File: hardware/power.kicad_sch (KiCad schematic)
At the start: 10 parts, among them J1 Conn_01x02_Pin, U2 TPS7A91

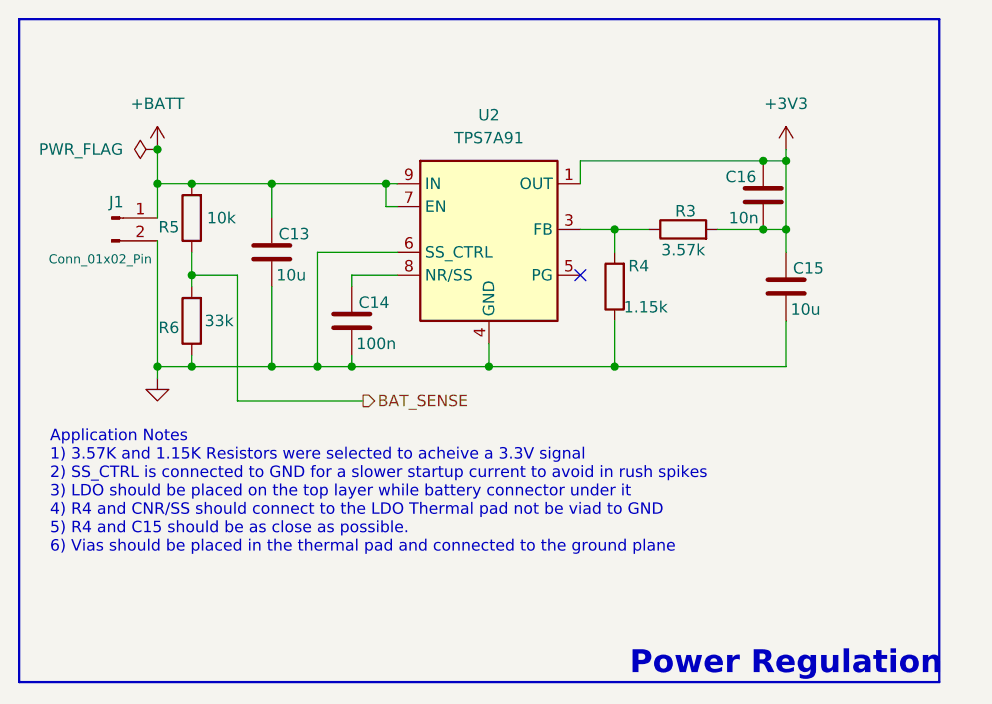
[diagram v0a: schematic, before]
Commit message: feat(kicad): Added step files for missing parts
changed flyback diode to SMA part with 5A max

Redid initial layout
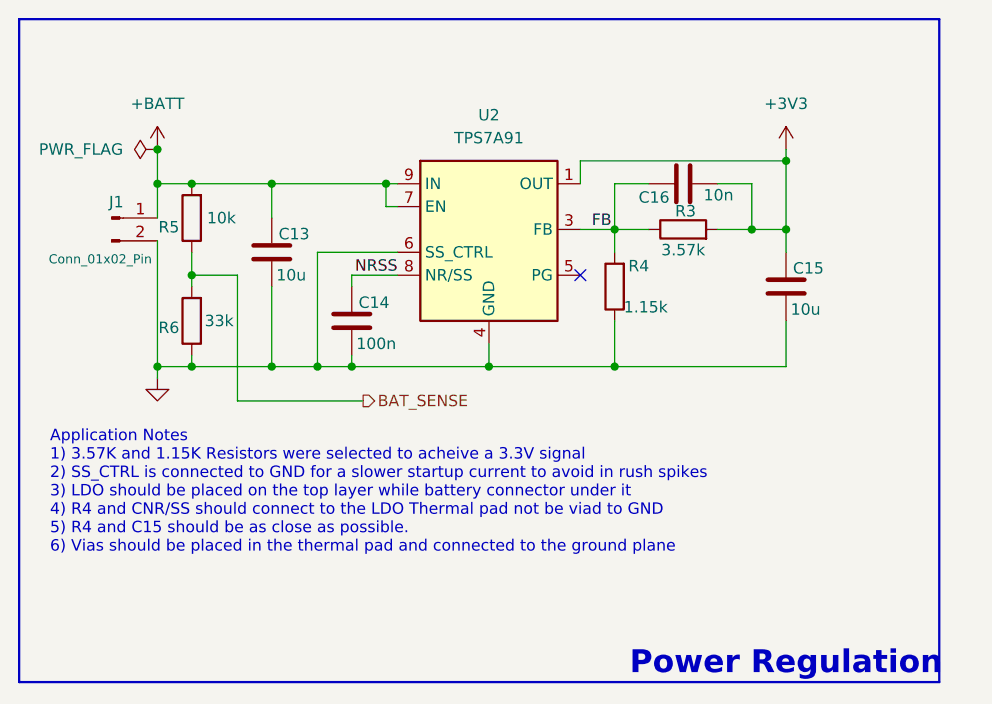
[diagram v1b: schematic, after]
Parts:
- U2: footprint Package_DFN_QFN:Texas_S-PDSO-N10_EP1.2x2mm -> Package_DFN_QFN:Texas_S-PDSO-N10_EP1.2x2mm_ThermalVias
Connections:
- net +3V3: no longer C16.1
- net NRSS: now reaches C14.1, U2.8 (NR/SS)
- net FB: now reaches R3.1, R4.2, U2.3 (FB)
- net FB: now also C16.1
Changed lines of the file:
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@@
+	)
+	(junction
+		(at 170.18 90.17)
+		(diameter 0)
+		(color 0 0 0 0)
 	)
 	(junction
@@
 	)
 	(junction
-		(at 171.45 90.17)
-		(diameter 0)
-		(color 0 0 0 0)
-	)
-	(junction
 		(at 107.95 85.09)
 		(diameter 0)
@@
 	(junction
 		(at 173.99 90.17)
-		(diameter 0)
-		(color 0 0 0 0)
-	)
-	(junction
-		(at 171.45 82.55)
 		(diameter 0)
 		(color 0 0 0 0)
@@
 	(wire
 		(pts
+			(xy 158.75 85.09) (xy 154.94 85.09)
+		)
+		(stroke
+			(width 0)
+			(type default)
+		)
+	)
+	(wire
+		(pts
 			(xy 107.95 104.14) (xy 107.95 105.41)
 		)
@@
 	(wire
 		(pts
-			(xy 171.45 82.55) (xy 173.99 82.55)
+			(xy 151.13 82.55) (xy 173.99 82.55)
 		)
 		(stroke
@@
 	(wire
 		(pts
-			(xy 151.13 82.55) (xy 171.45 82.55)
-		)
-		(stroke
-			(width 0)
-			(type default)
-		)
-	)
-	(wire
-		(pts
 			(xy 104.14 105.41) (xy 107.95 105.41)
 		)
@@
 	(wire
 		(pts
-			(xy 166.37 90.17) (xy 173.99 90.17)
+			(xy 166.37 90.17) (xy 170.18 90.17)
 		)
 		(stroke
@@
 	(wire
 		(pts
+			(xy 170.18 90.17) (xy 173.99 90.17)
+		)
+		(stroke
+			(width 0)
+			(type default)
+		)
+	)
+	(wire
+		(pts
 			(xy 127 109.22) (xy 113.03 109.22)
 		)
@@
 	(wire
 		(pts
+			(xy 170.18 85.09) (xy 170.18 90.17)
+		)
+		(stroke
+			(width 0)
+			(type default)
+		)
+	)
+	(wire
+		(pts
 			(xy 104.14 91.44) (xy 104.14 105.41)
 		)
@@
 	(wire
 		(pts
+			(xy 154.94 85.09) (xy 154.94 90.17)
+		)
+		(stroke
+			(width 0)
+			(type default)
+		)
+	)
+	(wire
+		(pts
 			(xy 173.99 100.33) (xy 173.99 105.41)
 		)
@@
 	(wire
 		(pts
+			(xy 166.37 85.09) (xy 170.18 85.09)
+		)
+		(stroke
+			(width 0)
+			(type default)
+		)
+	)
+	(wire
+		(pts
 			(xy 130.81 95.25) (xy 125.73 95.25)
 		)
@@
 			(width 0)
 			(type default)
+		)
+	)
+	(label "FB"
+		(at 152.4 90.17 0)
+		(effects
+			(font
+				(size 1.27 1.27)
+			)
+			(justify left bottom)
+		)
+	)
+	(label "NRSS"
+		(at 130.81 95.25 180)
+		(effects
+			(font
+				(size 1.27 1.27)
+			)
+			(justify right bottom)
 		)
 	)
@@
 	(symbol
 		(lib_id "Device:C")
-		(at 171.45 86.36 0)
-		(mirror y)
+		(at 162.56 85.09 90)
+		(mirror x)
 		(unit 1)
 		(body_style 1)
@@
 		(dnp no)
 		(property "Reference" "C16"
-			(at 170.688 84.328 0)
+			(at 161.036 86.614 90)
 			(show_name no)
 			(do_not_autoplace no)
@@
 		)
 		(property "Value" "10n"
-			(at 170.942 88.9 0)
+			(at 168.148 86.36 90)
 			(show_name no)
 			(do_not_autoplace no)
@@
 		)
 		(property "Footprint" "Capacitor_SMD:C_0402_1005Metric"
-			(at 170.4848 90.17 0)
+			(at 166.37 86.0552 0)
 			(hide yes)
 			(show_name no)
@@
 		)
 		(property "Datasheet" ""
-			(at 171.45 86.36 0)
+			(at 162.56 85.09 0)
 			(hide yes)
 			(show_name no)
@@
 		)
 		(property "Description" "Unpolarized capacitor"
-			(at 171.45 86.36 0)
+			(at 162.56 85.09 0)
 			(hide yes)
 			(show_name no)
@@
 			)
 		)
-		(property "Footprint" "Package_DFN_QFN:Texas_S-PDSO-N10_EP1.2x2mm"
+		(property "Footprint" "Package_DFN_QFN:Texas_S-PDSO-N10_EP1.2x2mm_ThermalVias"
 			(at 140.97 91.44 0)
 			(hide yes)

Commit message: feat(kicad): Routing complete, assigning jlc components to each footprint
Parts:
- C13, C15: LCSC (none) -> C19702
- C14: LCSC (none) -> C1525
- J1: LCSC (none) -> C173752
- R3: value 3.57k -> 4k7; LCSC (none) -> C25900
- R4: value 1.15k -> 1k5; LCSC (none) -> C25867
- R5: LCSC (none) -> C25744
- R6: LCSC (none) -> C25779
- U2: LCSC (none) -> C969024

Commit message: feat(kicad): Cleaned up routing and picked LCSC parts for several components
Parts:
- C16: LCSC (none) -> C15195
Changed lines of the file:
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@@
 			)
 		)
-		(property "LCSC" ""
+		(property "LCSC" "C15195"
 			(at 162.56 85.09 90)
 			(hide yes)
